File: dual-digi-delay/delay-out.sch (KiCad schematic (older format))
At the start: 11 parts, among them U8 TL072

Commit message: Final revision of dual digi delay
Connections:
- net DELAY1_WET: now also U8.3 (+); no longer U8.5 (+)
- net DELAY1_WET_OUT: now also R63.1; no longer R62.1
- net DELAY2_WET: now also U8.5 (+); no longer U8.3 (+)
- net DELAY2_WET_OUT: now also R62.1; no longer R63.1
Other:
- moved on the sheet: C52, C55, R56, R57, R58, R59, R62, R63, U8A, U8B

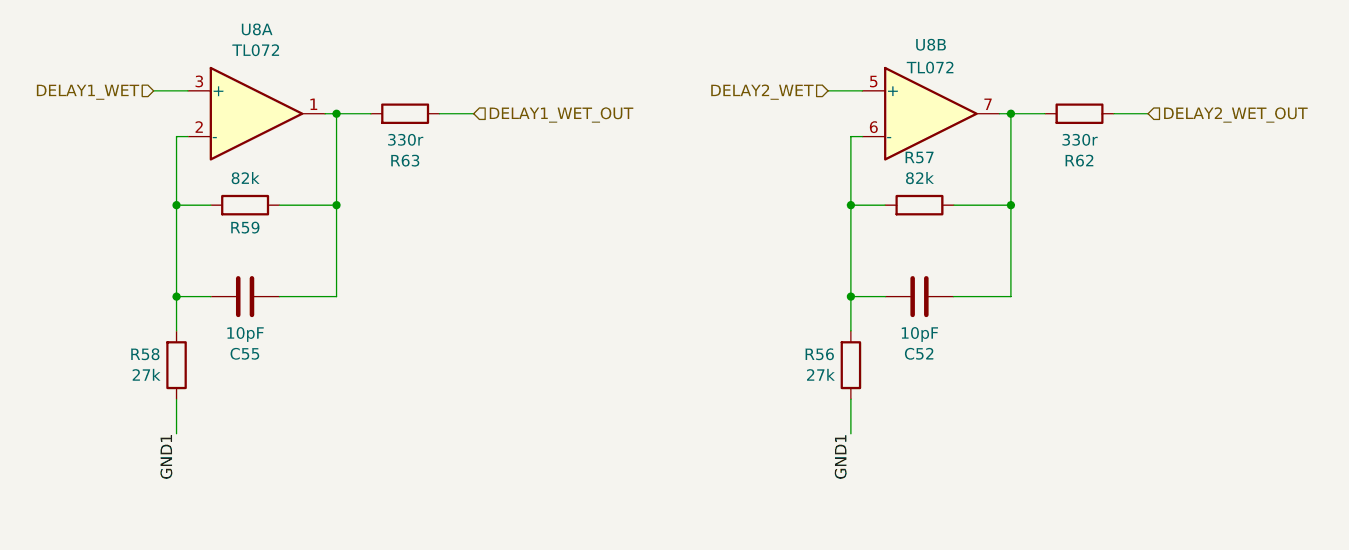
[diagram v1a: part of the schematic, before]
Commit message: Updating digi delay to rev 2
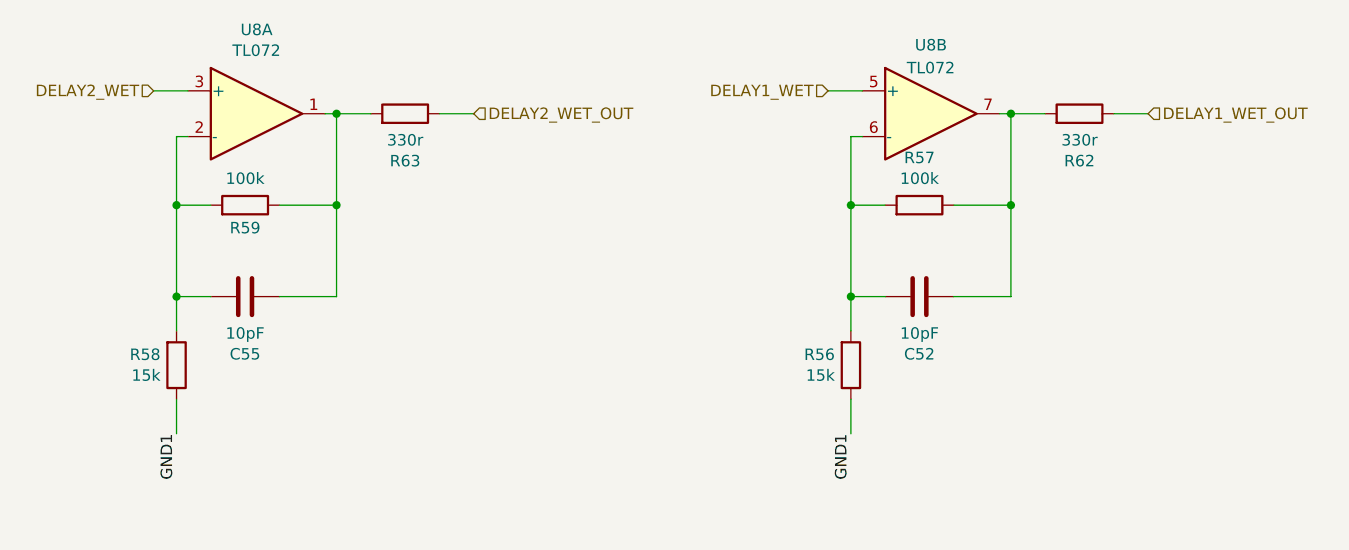
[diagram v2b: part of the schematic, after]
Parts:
- R56, R58: value 27k -> 15k
- R57, R59: value 82k -> 100k
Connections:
- net DELAY1_WET: now also U8.5 (+); no longer U8.3 (+)
- net DELAY1_WET_OUT: now also R62.1; no longer R63.1
- net DELAY2_WET: now also U8.3 (+); no longer U8.5 (+)
- net DELAY2_WET_OUT: now also R63.1; no longer R62.1
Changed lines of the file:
@@
 $Descr A4 11693 8268
 encoding utf-8
-Sheet 8 10
+Sheet 7 11
 Title ""
 Date ""
@@
 P 3450 2800
 F 0 "R58" H 3380 2754 50  0000 R CNN
-F 1 "27k" H 3380 2845 50  0000 R CNN
+F 1 "15k" H 3380 2845 50  0000 R CNN
 F 2 "rumblesan-footprints:Resistor_THT_L6.3mm_D2.5mm_P10.16mm_Horizontal" V 3380 2800 50  0001 C CNN
 F 3 "~" H 3450 2800 50  0001 C CNN
@@
 P 3750 2100
 F 0 "R59" V 3650 2100 50  0000 C CNN
-F 1 "82k" V 3866 2100 50  0000 C CNN
+F 1 "100k" V 3866 2100 50  0000 C CNN
 F 2 "rumblesan-footprints:Resistor_THT_L6.3mm_D2.5mm_P10.16mm_Horizontal" V 3680 2100 50  0001 C CNN
 F 3 "~" H 3750 2100 50  0001 C CNN
@@
 	1    0    0    -1
 $EndComp
-Text HLabel 3350 1600 0    50   Input ~ 0
+Text HLabel 6300 1600 0    50   Input ~ 0
 DELAY1_WET
 $Comp
@@
 Wire Wire Line
 	4450 5750 4300 5750
-Text HLabel 4750 1700 2    50   Input ~ 0
+Text HLabel 7700 1700 2    50   Input ~ 0
 DELAY1_WET_OUT
 $Comp
@@
 	0    1    -1   0
 $EndComp
-Text HLabel 7700 1700 2    50   Input ~ 0
+Text HLabel 4750 1700 2    50   Input ~ 0
 DELAY2_WET_OUT
 Text Label 4250 4050 2    50   ~ 0
@@
 Text Label 6400 3100 3    50   ~ 0
 GND1
-Text HLabel 6300 1600 0    50   Input ~ 0
+Text HLabel 3350 1600 0    50   Input ~ 0
 DELAY2_WET
 Wire Wire Line
@@
 AR Path="/621CDCC0/62263431" Ref="R57"  Part="1"
 F 0 "R57" V 6907 2100 50  0000 C CNN
-F 1 "82k" V 6816 2100 50  0000 C CNN
+F 1 "100k" V 6816 2100 50  0000 C CNN
 F 2 "rumblesan-footprints:Resistor_THT_L6.3mm_D2.5mm_P10.16mm_Horizontal" V 6630 2100 50  0001 C CNN
 F 3 "~" H 6700 2100 50  0001 C CNN
@@
 AR Path="/621CDCC0/62263411" Ref="R56"  Part="1"
 F 0 "R56" H 6330 2754 50  0000 R CNN
-F 1 "27k" H 6330 2845 50  0000 R CNN
+F 1 "15k" H 6330 2845 50  0000 R CNN
 F 2 "rumblesan-footprints:Resistor_THT_L6.3mm_D2.5mm_P10.16mm_Horizontal" V 6330 2800 50  0001 C CNN
 F 3 "~" H 6400 2800 50  0001 C CNN
